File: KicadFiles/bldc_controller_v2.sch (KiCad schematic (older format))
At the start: 175 parts, among them J1 Conn_01x05_Male, J10 Conn_01x02_Female, J11 Conn_01x02_Female, J12 Conn_01x02_Female, J13 Conn_01x02_Female, J14 Conn_01x02_Female, J15 Conn_01x04_Male, J2 Conn_01x03_Male, J3 Conn_01x03_Male, J4 1935174, J5 Conn_01x02_Female, J9 Conn_01x02_Female, Q10 IRLB8721PBF, Q11 IRLB8721PBF, Q2 DMN65D8L-7, Q3 DMN65D8L-7, Q5 IRF4905, Q6 IRLB8721PBF, Q7 IRLB8721PBF, Q8 IRLB8721PBF, Q9 IRLB8721PBF, SW2 D6C40 F1 LFS, SW3 1301.9314, SW4 1301.9314, SW5 SW_Push_DPDT, U1 ATmega328P-PU, U2 uA7810, U3 LM7805_TO220, U4 MCP601-xP, U5 LM339, U6 IRS2004, U7 IRS2004, U8 IRS2004, U9 HCPL-181-00DE, Y1 9B-16.000MBBK-B

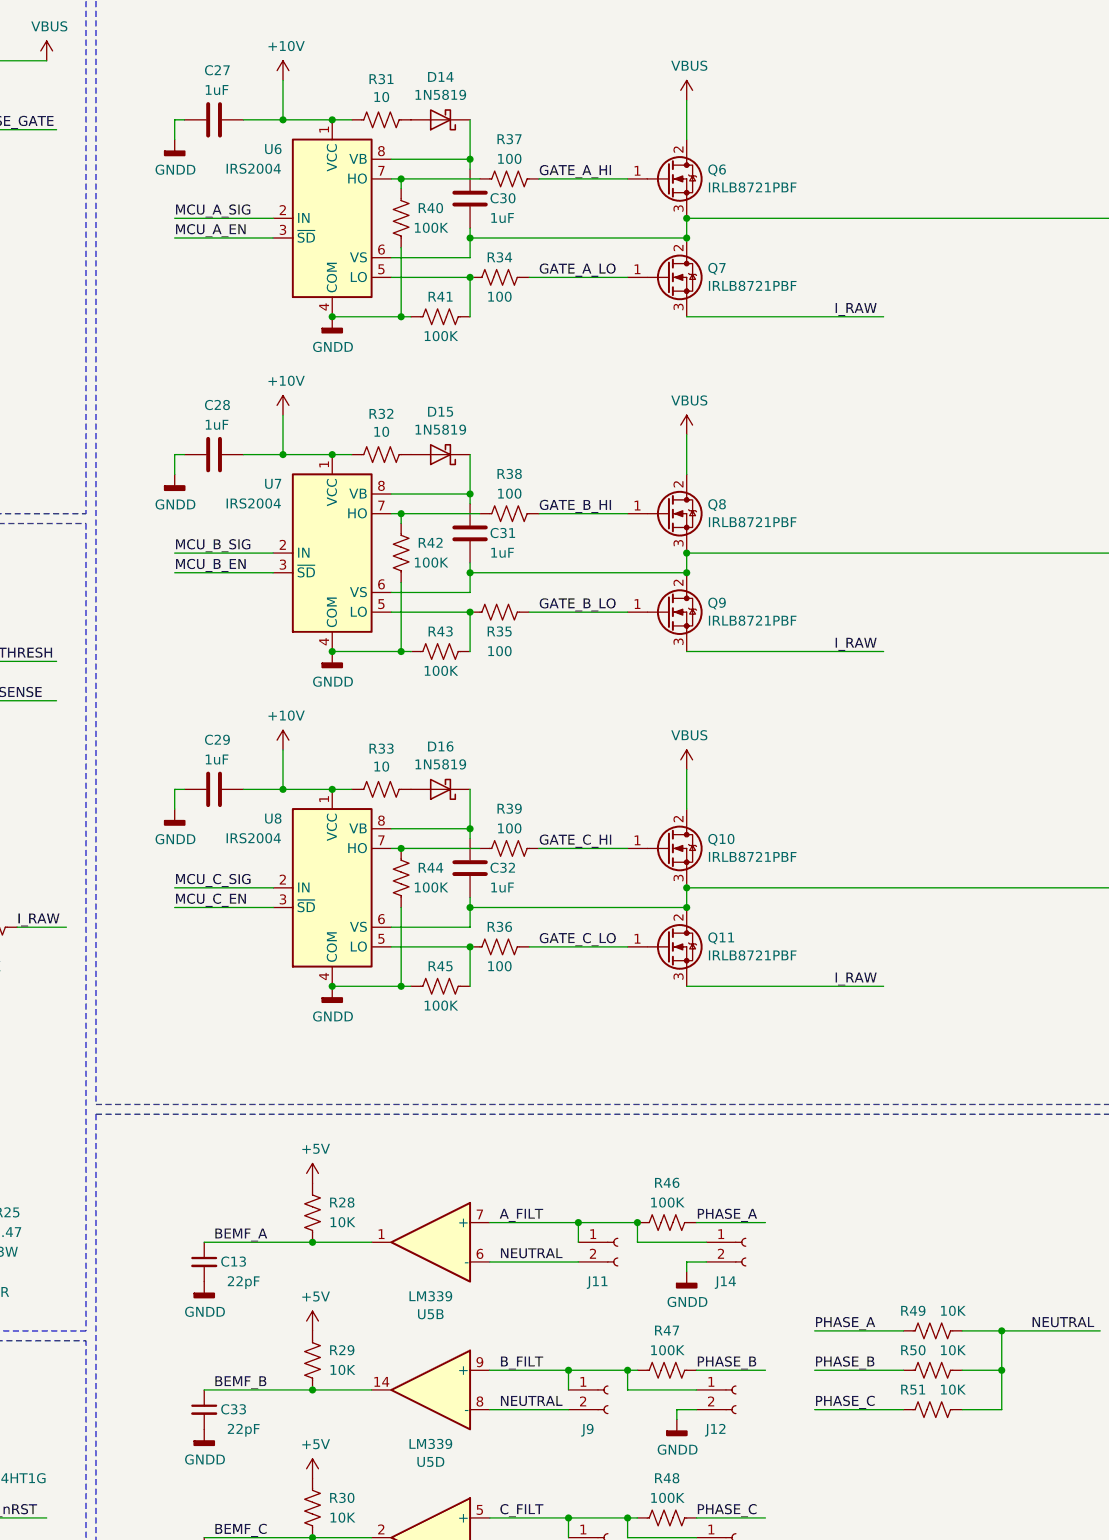
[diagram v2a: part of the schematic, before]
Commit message: Updated Power Ground
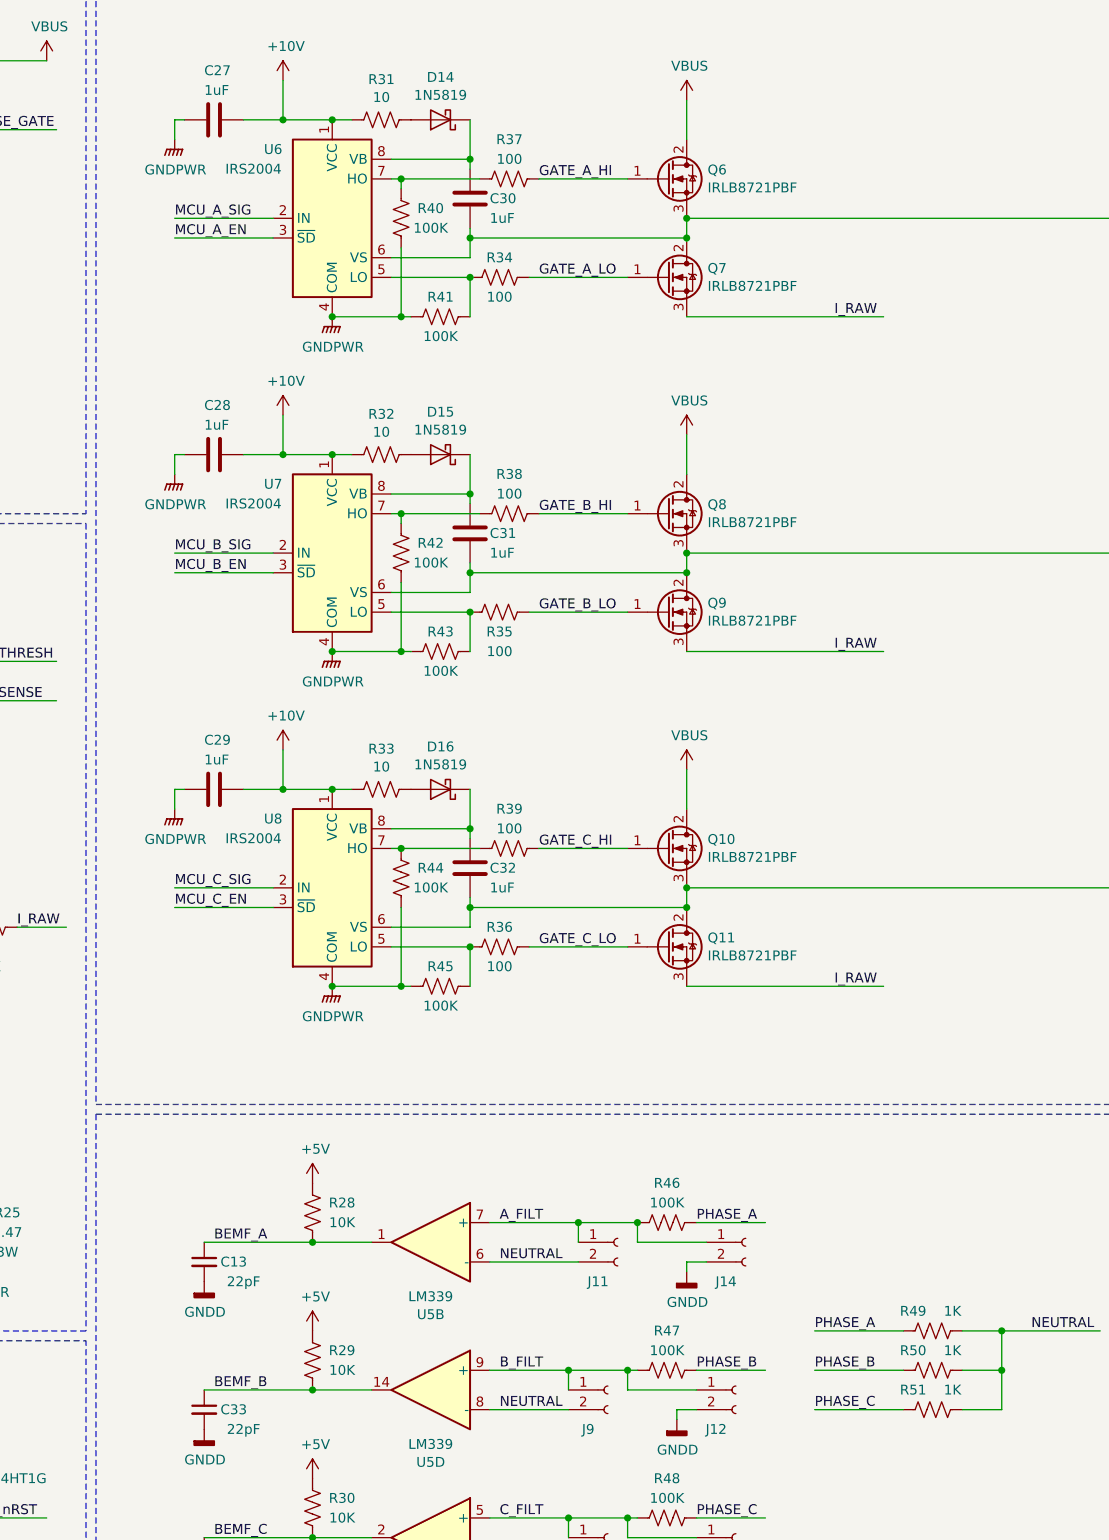
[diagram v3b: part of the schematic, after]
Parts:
- R49, R50, R51: value 10K -> 1K
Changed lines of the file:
@@
 Comment4 ""
 $EndDescr
-$Comp
-L power:GNDD #PWR0100
-U 1 1 5DCB3729
-P 11150 2300
-F 0 "#PWR0100" H 11150 2050 50  0001 C CNN
-F 1 "GNDD" H 11154 2145 50  0000 C CNN
-F 2 "" H 11150 2300 50  0001 C CNN
-F 3 "" H 11150 2300 50  0001 C CNN
-	1    11150 2300
-	1    0    0    -1
-$EndComp
 Wire Wire Line
 	10700 1300 10900 1300
@@
 	0    -1   1    0
 $EndComp
-$Comp
-L power:GNDD #PWR091
-U 1 1 5DBEA732
-P 10350 1400
-F 0 "#PWR091" H 10350 1150 50  0001 C CNN
-F 1 "GNDD" H 10354 1245 50  0000 C CNN
-F 2 "" H 10350 1400 50  0001 C CNN
-F 3 "" H 10350 1400 50  0001 C CNN
-	1    10350 1400
-	1    0    0    -1
-$EndComp
 Wire Wire Line
 	10350 1400 10350 1300
@@
 P 14200 7450
 F 0 "R49" V 14100 7350 50  0000 C CNN
-F 1 "10K" V 14100 7550 50  0000 C CNN
+F 1 "1K" V 14100 7550 50  0000 C CNN
 F 2 "Resistor_SMD:R_0805_2012Metric_Pad1.15x1.40mm_HandSolder" V 14240 7440 50  0001 C CNN
 F 3 "~" H 14200 7450 50  0001 C CNN
@@
 P 14200 7650
 F 0 "R50" V 14100 7550 50  0000 C CNN
-F 1 "10K" V 14100 7750 50  0000 C CNN
+F 1 "1K" V 14100 7750 50  0000 C CNN
 F 2 "Resistor_SMD:R_0805_2012Metric_Pad1.15x1.40mm_HandSolder" V 14240 7640 50  0001 C CNN
 F 3 "~" H 14200 7650 50  0001 C CNN
@@
 P 14200 7850
 F 0 "R51" V 14100 7750 50  0000 C CNN
-F 1 "10K" V 14100 7950 50  0000 C CNN
+F 1 "1K" V 14100 7950 50  0000 C CNN
 F 2 "Resistor_SMD:R_0805_2012Metric_Pad1.15x1.40mm_HandSolder" V 14240 7840 50  0001 C CNN
 F 3 "~" H 14200 7850 50  0001 C CNN
@@
 Text Label 12200 2100 0    50   ~ 0
 GATE_A_LO
-$Comp
-L power:GNDD #PWR0101
-U 1 1 6071FDBB
-P 11150 4000
-F 0 "#PWR0101" H 11150 3750 50  0001 C CNN
-F 1 "GNDD" H 11154 3845 50  0000 C CNN
-F 2 "" H 11150 4000 50  0001 C CNN
-F 3 "" H 11150 4000 50  0001 C CNN
-	1    11150 4000
-	1    0    0    -1
-$EndComp
 Wire Wire Line
 	10700 3000 10900 3000
@@
 	0    -1   1    0
 $EndComp
-$Comp
-L power:GNDD #PWR092
-U 1 1 6071FDD1
-P 10350 3100
-F 0 "#PWR092" H 10350 2850 50  0001 C CNN
-F 1 "GNDD" H 10354 2945 50  0000 C CNN
-F 2 "" H 10350 3100 50  0001 C CNN
-F 3 "" H 10350 3100 50  0001 C CNN
-	1    10350 3100
-	1    0    0    -1
-$EndComp
 Wire Wire Line
 	10350 3100 10350 3000
@@
 Text Label 12200 3800 0    50   ~ 0
 GATE_B_LO
-$Comp
-L power:GNDD #PWR0102
-U 1 1 60799BBF
-P 11150 5700
-F 0 "#PWR0102" H 11150 5450 50  0001 C CNN
-F 1 "GNDD" H 11154 5545 50  0000 C CNN
-F 2 "" H 11150 5700 50  0001 C CNN
-F 3 "" H 11150 5700 50  0001 C CNN
-	1    11150 5700
-	1    0    0    -1
-$EndComp
 Wire Wire Line
 	10700 4700 10900 4700
@@
 	0    -1   1    0
 $EndComp
-$Comp
-L power:GNDD #PWR093
-U 1 1 60799BD5
-P 10350 4800
-F 0 "#PWR093" H 10350 4550 50  0001 C CNN
-F 1 "GNDD" H 10354 4645 50  0000 C CNN
-F 2 "" H 10350 4800 50  0001 C CNN
-F 3 "" H 10350 4800 50  0001 C CNN
-	1    10350 4800
-	1    0    0    -1
-$EndComp
 Wire Wire Line
 	10350 4800 10350 4700
@@
 Wire Wire Line
 	11550 2300 11500 2300
-Connection ~ 11150 2300
 $Comp
 L Device:R_US R41
@@
 Wire Wire Line
 	11500 4000 11150 4000
-Connection ~ 11150 4000
 Wire Wire Line
 	11450 2000 11850 2000
@@
 Wire Wire Line
 	11500 5300 11500 5700
-Connection ~ 11150 5700
 Wire Wire Line
 	11150 5700 11500 5700
@@
 	1    0    0    -1
 $EndComp
+$Comp
+L power:GNDPWR #PWR0101
+U 1 1 5E177BA2
+P 10350 1400
+F 0 "#PWR0101" H 10350 1200 50  0001 C CNN
+F 1 "GNDPWR" H 10354 1246 50  0000 C CNN
+F 2 "" H 10350 1350 50  0001 C CNN
+F 3 "" H 10350 1350 50  0001 C CNN
+	1    10350 1400
+	1    0    0    -1
+$EndComp
+$Comp
+L power:GNDPWR #PWR0102
+U 1 1 5E17938B
+P 11150 2300
+F 0 "#PWR0102" H 11150 2100 50  0001 C CNN
+F 1 "GNDPWR" H 11154 2146 50  0000 C CNN
+F 2 "" H 11150 2250 50  0001 C CNN
+F 3 "" H 11150 2250 50  0001 C CNN
+	1    11150 2300
+	1    0    0    -1
+$EndComp
+Connection ~ 11150 2300
+$Comp
+L power:GNDPWR #PWR0106
+U 1 1 5E179E8A
+P 10350 3100
+F 0 "#PWR0106" H 10350 2900 50  0001 C CNN
+F 1 "GNDPWR" H 10354 2946 50  0000 C CNN
+F 2 "" H 10350 3050 50  0001 C CNN
+F 3 "" H 10350 3050 50  0001 C CNN
+	1    10350 3100
+	1    0    0    -1
+$EndComp
+$Comp
+L power:GNDPWR #PWR0107
+U 1 1 5E17A5F6
+P 11150 4000
+F 0 "#PWR0107" H 11150 3800 50  0001 C CNN
+F 1 "GNDPWR" H 11154 3846 50  0000 C CNN
+F 2 "" H 11150 3950 50  0001 C CNN
+F 3 "" H 11150 3950 50  0001 C CNN
+	1    11150 4000
+	1    0    0    -1
+$EndComp
+$Comp
+L power:GNDPWR #PWR0108
+U 1 1 5E17D707
+P 10350 4800
+F 0 "#PWR0108" H 10350 4600 50  0001 C CNN
+F 1 "GNDPWR" H 10354 4646 50  0000 C CNN
+F 2 "" H 10350 4750 50  0001 C CNN
+F 3 "" H 10350 4750 50  0001 C CNN
+	1    10350 4800
+	1    0    0    -1
+$EndComp
+$Comp
+L power:GNDPWR #PWR0109
+U 1 1 5E17DE22
+P 11150 5700
+F 0 "#PWR0109" H 11150 5500 50  0001 C CNN
+F 1 "GNDPWR" H 11154 5546 50  0000 C CNN
+F 2 "" H 11150 5650 50  0001 C CNN
+F 3 "" H 11150 5650 50  0001 C CNN
+	1    11150 5700
+	1    0    0    -1
+$EndComp
+Connection ~ 11150 5700
+Connection ~ 11150 4000
 $EndSCHEMATC
